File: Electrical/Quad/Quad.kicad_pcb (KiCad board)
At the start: 2 copper layers, 140 x 70 mm, 132 parts, among them J101 01x04, J102 01x04, J103 01x03, J104 01x03, J201 01x03, J202 01x04, J203 01x03, J204 01x04, J205 01x03, J206 USB_OTG, J207 01x04, J208 01x02, J209 01x04, J210 01x02, J211 01x02, J212 4PostTerm, J213 2PostTerm, J214 2PostTerm, J215 2PostTerm, J216 2PostTerm, J217 2PostTerm, J218 01x02, J219 01x02, Q201 FDC6420C, Q202 FDG1024NZ, Q301 FDC6420C, Q401 FDC6420C, Q501 FDC6420C, Q601 FDC6420C, U201 TPD4S012, U202 ACS712ELCTR-05B-T, U203 ACS712ELCTR-05B-T, U204 24LC256, U205 LM2576HVS-ADJ, U206 LM2576HVS-ADJ

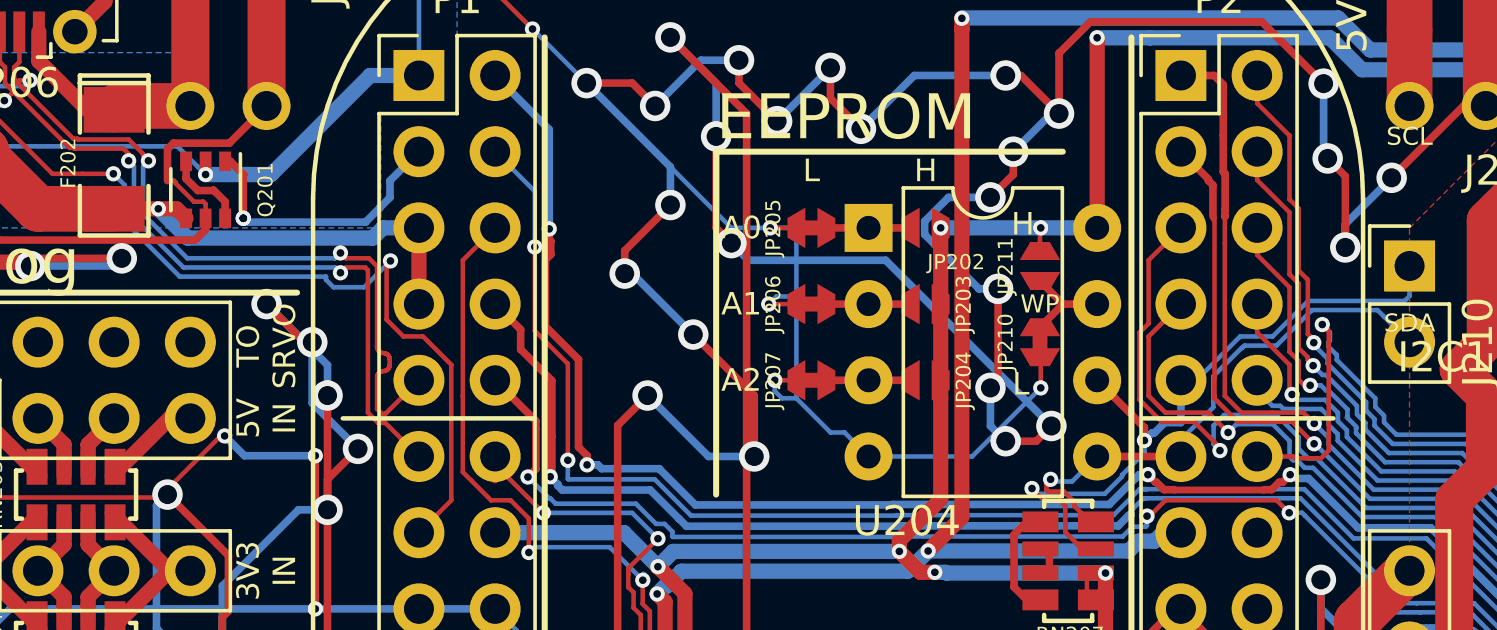
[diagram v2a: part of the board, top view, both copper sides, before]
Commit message: Fixed DRC errors
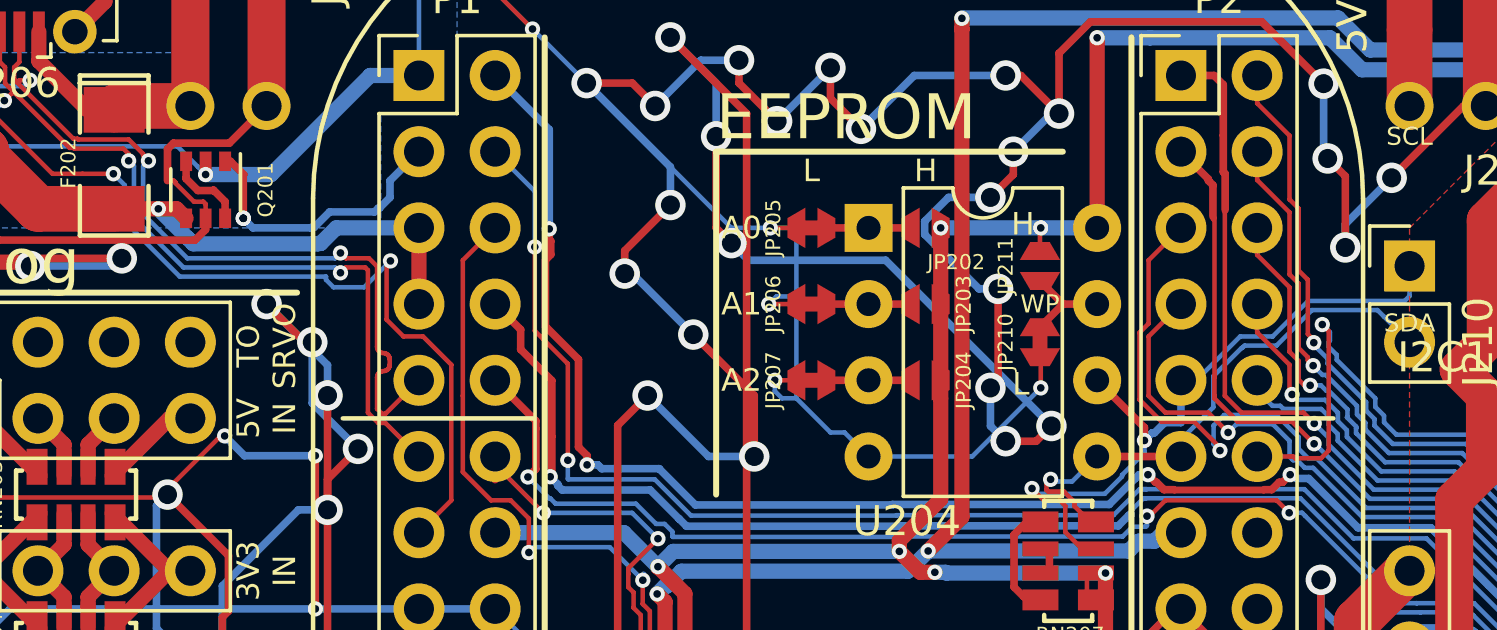
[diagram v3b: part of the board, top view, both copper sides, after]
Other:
- net class Default: clearance 0.1524 -> 0.152146
- net class Minimum: clearance 0.1524 -> 0.152146
- rule trace_clearance: 0.1524 -> 0.152146
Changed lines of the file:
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@@
   (general
     (links 606)
-    (no_connects 1)
-    (area 29.695199 64.695199 170.304801 135.304801)
+    (no_connects 0)
+    (area 13.150001 57.061 175.794287 147.700001)
     (thickness 1.6)
     (drawings 192)
-    (tracks 5409)
+    (tracks 5415)
     (zones 0)
     (modules 132)
@@
   )
   (setup
-    (last_trace_width 0.254)
+    (last_trace_width 0.1524)
     (user_trace_width 0.1524)
     (user_trace_width 0.254)
@@
     (user_trace_width 2.54)
     (user_trace_width 5.08)
-    (trace_clearance 0.1524)
+    (trace_clearance 0.152146)
     (zone_clearance 0.1524)
     (zone_45_only no)
@@
   (net 152 /pr1_pru1_pru_r30_11)
   (net_class Default "This is the default net class."
-    (clearance 0.1524)
+    (clearance 0.152146)
     (trace_width 0.254)
     (via_dia 0.508)
@@
   )
   (net_class Minimum ""
-    (clearance 0.1524)
+    (clearance 0.152146)
     (trace_width 0.1524)
     (via_dia 0.508)
@@
   (segment (start 52.511599 127.296401) (end 51.328 128.48) (width 0.508) (layer F.Cu) (net 68))
   (segment (start 51.328 128.48) (end 51.328 129.588) (width 0.508) (layer F.Cu) (net 68))
+  (segment (start 82.422139 75.868521) (end 80.492922 75.868521) (width 0.254) (layer B.Cu) (net 69))
+  (segment (start 80.492922 75.868521) (end 80.174402 75.550001) (width 0.254) (layer B.Cu) (net 69))
+  (segment (start 83.052172 75.336845) (end 82.532813 75.856204) (width 0.254) (layer B.Cu) (net 69))
+  (segment (start 82.532813 75.856204) (end 82.434456 75.856204) (width 0.254) (layer B.Cu) (net 69))
+  (segment (start 82.434456 75.856204) (end 82.422139 75.868521) (width 0.254) (layer B.Cu) (net 69))
+  (segment (start 84.548936 75.336844) (end 83.052172 75.336845) (width 0.254) (layer B.Cu) (net 69))
+  (segment (start 84.719391 75.2096) (end 84.67618 75.2096) (width 0.254) (layer B.Cu) (net 69))
+  (segment (start 84.67618 75.2096) (end 84.548936 75.336844) (width 0.254) (layer B.Cu) (net 69))
   (segment (start 85.0648 74.854) (end 85.0648 74.2952) (width 0.254) (layer B.Cu) (net 69))
   (segment (start 85.0648 74.2952) (end 86.03 73.33) (width 0.254) (layer B.Cu) (net 69))
   (segment (start 84.719391 75.199409) (end 85.0648 74.854) (width 0.254) (layer B.Cu) (net 69))
   (segment (start 84.719391 75.2096) (end 84.719391 75.199409) (width 0.254) (layer B.Cu) (net 69))
-  (segment (start 84.719391 75.2096) (end 84.252 75.676991) (width 0.254) (layer B.Cu) (net 69))
-  (segment (start 84.252 75.676991) (end 80.3404 75.676991) (width 0.254) (layer B.Cu) (net 69))
-  (segment (start 80.3404 75.676991) (end 80.21341 75.550001) (width 0.254) (layer B.Cu) (net 69))
   (segment (start 80.21341 75.550001) (end 80.174402 75.550001) (width 0.254) (layer B.Cu) (net 69))
   (segment (start 80.188 74.092) (end 80.174402 74.105598) (width 0.254) (layer F.Cu) (net 69))
@@
   (segment (start 58.09 96.19) (end 59.835 96.19) (width 0.254) (layer F.Cu) (net 92))
   (segment (start 59.835 96.19) (end 60.47 96.825) (width 0.254) (layer F.Cu) (net 92))
+  (segment (start 86.03 75.87) (end 83.273013 75.87) (width 0.508) (layer B.Cu) (net 93))
+  (segment (start 83.273013 75.87) (end 82.753653 76.38936) (width 0.508) (layer B.Cu) (net 93))
+  (segment (start 82.753653 76.38936) (end 82.66584 76.38936) (width 0.508) (layer B.Cu) (net 93))
+  (segment (start 82.66584 76.38936) (end 82.653523 76.401677) (width 0.508) (layer B.Cu) (net 93))
+  (segment (start 82.653523 76.401677) (end 78.509877 76.401677) (width 0.508) (layer B.Cu) (net 93))
+  (segment (start 78.509877 76.401677) (end 78.318601 76.210401) (width 0.508) (layer B.Cu) (net 93))
+  (segment (start 78.318601 76.210401) (end 77.3432 75.235) (width 0.508) (layer B.Cu) (net 93))
   (segment (start 75.87 75.235) (end 73.33 75.235) (width 1.524) (layer F.Cu) (net 93))
   (segment (start 73.33 75.235) (end 71.6028 73.5078) (width 1.524) (layer F.Cu) (net 93))
@@
   (segment (start 75.87 75.235) (end 77.3432 75.235) (width 0.508) (layer F.Cu) (net 93))
   (segment (start 77.3432 75.235) (end 77.953 75.235) (width 0.508) (layer F.Cu) (net 93))
-  (segment (start 86.03 75.87) (end 84.827919 75.87) (width 0.508) (layer B.Cu) (net 93))
-  (segment (start 84.487518 76.210401) (end 78.318601 76.210401) (width 0.508) (layer B.Cu) (net 93))
   (via (at 77.3432 75.235) (size 0.508) (drill 0.254) (layers F.Cu B.Cu) (net 93))
-  (segment (start 84.827919 75.87) (end 84.487518 76.210401) (width 0.508) (layer B.Cu) (net 93))
-  (segment (start 78.318601 76.210401) (end 77.3432 75.235) (width 0.508) (layer B.Cu) (net 93))
   (segment (start 67.75 72.306) (end 67.488 72.568) (width 0.254) (layer F.Cu) (net 93))
   (segment (start 68.691 72.306) (end 67.75 72.306) (width 0.254) (layer F.Cu) (net 93))
@@
   (segment (start 112.3444 74.2952) (end 112.49679 74.44759) (width 0.254) (layer F.Cu) (net 128))
   (segment (start 111.43 73.33) (end 112.3444 74.2444) (width 0.254) (layer F.Cu) (net 128))
+  (segment (start 112.9032 75.265286) (end 112.9032 75.340845) (width 0.1524) (layer F.Cu) (net 129))
+  (segment (start 112.9032 75.340845) (end 112.891399 75.352646) (width 0.1524) (layer F.Cu) (net 129))
+  (segment (start 112.891399 75.352646) (end 112.891399 81.467729) (width 0.1524) (layer F.Cu) (net 129))
+  (segment (start 115.873087 82.388967) (end 115.512721 82.028601) (width 0.1524) (layer F.Cu) (net 129))
+  (segment (start 115.512721 82.028601) (end 113.452271 82.028601) (width 0.1524) (layer F.Cu) (net 129))
+  (segment (start 113.452271 82.028601) (end 112.891399 81.467729) (width 0.1524) (layer F.Cu) (net 129))
+  (segment (start 112.891399 75.277087) (end 112.9032 75.265286) (width 0.1524) (layer F.Cu) (net 129))
   (segment (start 140.447 89.19) (end 140.795 89.19) (width 0.254) (layer F.Cu) (net 129))
   (segment (start 140.795 89.19) (end 141.91 90.305) (width 0.254) (layer F.Cu) (net 129))
@@
   (segment (start 141.92016 90.31516) (end 141.91 90.305) (width 0.1524) (layer F.Cu) (net 129))
   (via (at 141.92016 90.48763) (size 0.508) (drill 0.254) (layers F.Cu B.Cu) (net 129))
-  (segment (start 114.478899 82.028601) (end 115.512721 82.028601) (width 0.1524) (layer F.Cu) (net 129))
-  (segment (start 115.512721 82.028601) (end 115.873087 82.388967) (width 0.1524) (layer F.Cu) (net 129))
   (via (at 115.873087 82.388967) (size 0.508) (drill 0.254) (layers F.Cu B.Cu) (net 129))
-  (segment (start 113.452271 82.028601) (end 114.478899 82.028601) (width 0.1524) (layer F.Cu) (net 129))
-  (segment (start 112.891399 76.387729) (end 112.891399 81.467729) (width 0.1524) (layer F.Cu) (net 129))
-  (segment (start 112.891399 81.467729) (end 113.452271 82.028601) (width 0.1524) (layer F.Cu) (net 129))
-  (segment (start 112.9032 75.265286) (end 112.891399 75.489) (width 0.254) (layer F.Cu) (net 129))
-  (segment (start 112.891399 75.489) (end 112.9032 75.489) (width 0.254) (layer F.Cu) (net 129))
-  (segment (start 112.891399 76.387729) (end 112.891399 75.489) (width 0.1524) (layer F.Cu) (net 129))
-  (segment (start 112.891399 75.500801) (end 112.9032 75.489) (width 0.1524) (layer F.Cu) (net 129))
   (segment (start 112.9032 74.0666) (end 112.9032 75.265286) (width 0.254) (layer F.Cu) (net 129))
   (segment (start 112.840599 74.003999) (end 112.9032 74.0666) (width 0.254) (layer F.Cu) (net 129))

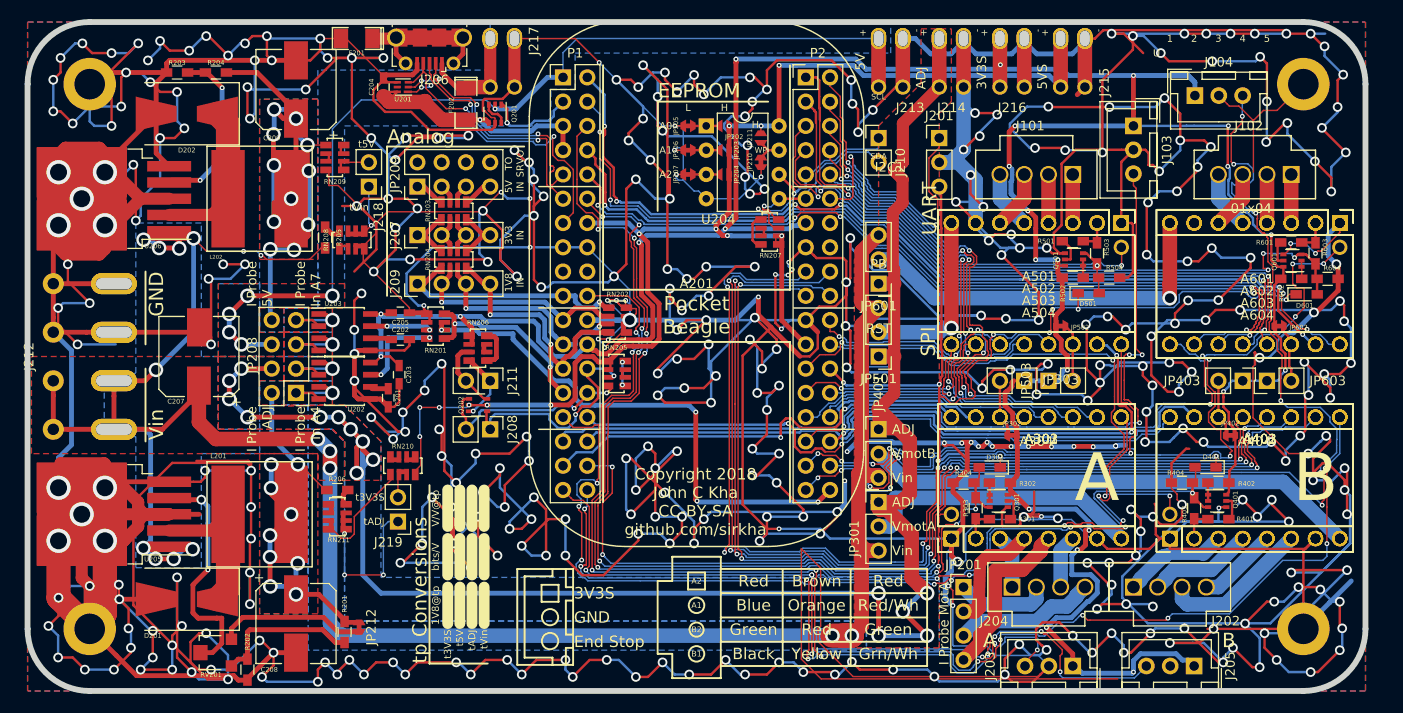
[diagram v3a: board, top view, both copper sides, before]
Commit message: Fixed silkscreen errors and other minor improvements to trace layouts.
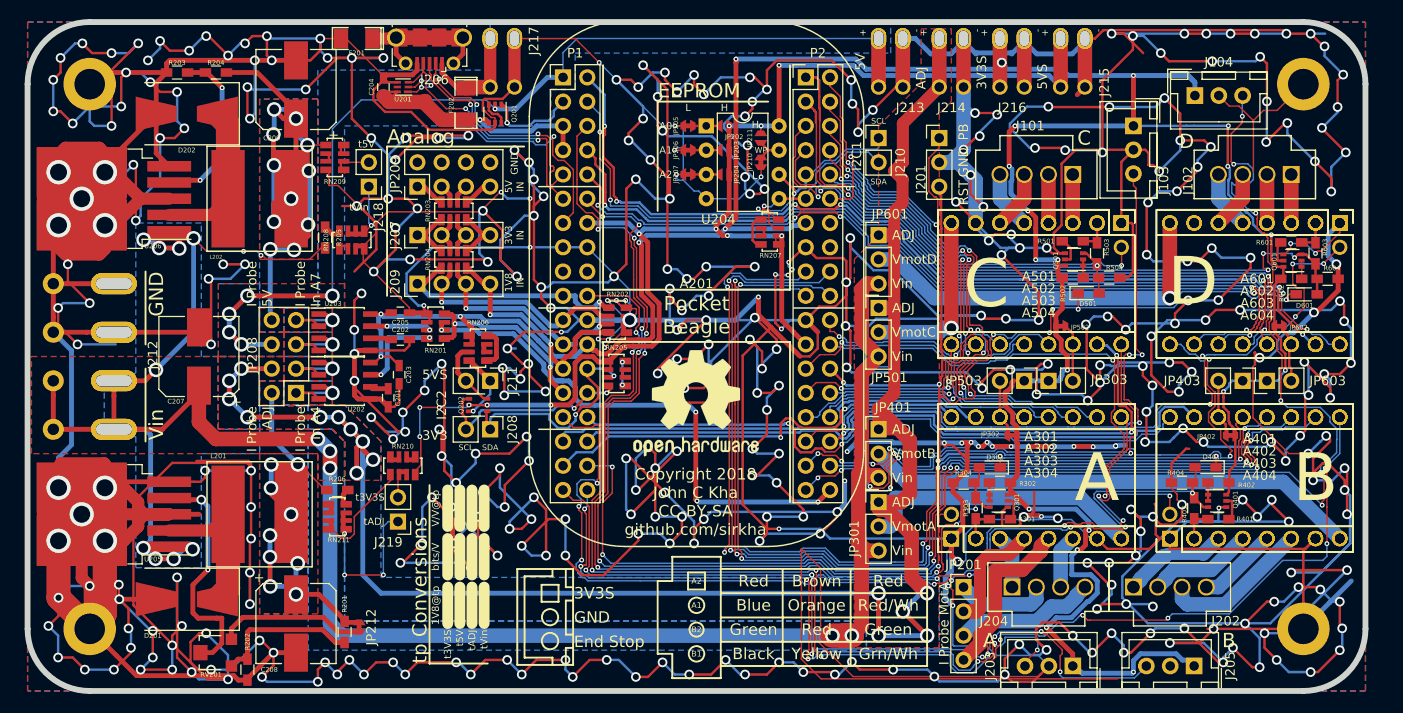
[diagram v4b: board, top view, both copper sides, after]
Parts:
- added REF***: OSHW-Logo2_14.6x12mm_SilkScreen, Symbols:OSHW-Logo2_14.6x12mm_SilkScreen, F.Cu at (99.9, 104.9)
- moved JP501 5.08 mm to (119.0, 94.9), turned to 0 degrees
- moved JP601 5.08 mm to (119.0, 87.3), turned to 0 degrees
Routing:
- net GND: track 2830.6 -> 2865.7 mm, vias 419 -> 427
- net /pr1_pru1_pru_r30_09: track 107.6 -> 99.6 mm
- net Vin: track 243.9 -> 239.8 mm
- net 3V3S: track 355.2 -> 357.9 mm
- net /Common/ain3: track 26.5 -> 25.4 mm
- net /Common/ain2: track 23.9 -> 23.0 mm
- net 5VS: track 134.2 -> 133.3 mm
- net /Common/ain7: track 55.8 -> 56.7 mm
- net /Common/ain1: track 23.6 -> 24.2 mm
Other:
- board text added: "3V3"
- board text added: "C"
- board text added: "D"
- board text added: "I2C2"
- board text added: "VmotC"
- board text added: "VmotD"
- board text removed: "SPI"
- board text removed: "TO SRVO"
- board text removed: "UART"

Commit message: Made pin one consistantly SCL on both sets of I2C headers.
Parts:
- moved J208 2.54 mm to (75.9, 107.6), turned to 90 degrees
- moved J211 2.54 mm to (75.9, 102.5), turned to 90 degrees
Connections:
- J208 pad 1: /Common/i2c2_sda -> /Common/i2c2_scl
- J208 pad 2: /Common/i2c2_scl -> /Common/i2c2_sda
- Q202 pad 3: Net-(J211-Pad1) -> Net-(J211-Pad2)
- Q202 pad 6: Net-(J211-Pad2) -> Net-(J211-Pad1)
- RN206 pad 3: Net-(J211-Pad2) -> Net-(J211-Pad1)
- RN206 pad 4: Net-(J211-Pad1) -> Net-(J211-Pad2)
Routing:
- net Net-(J211-Pad2): track 7.55 -> 7.43 mm, vias 0 -> 1
- net Net-(J211-Pad1): track 7.43 -> 7.55 mm, vias 1 -> 0
